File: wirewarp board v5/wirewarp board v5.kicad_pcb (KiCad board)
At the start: 2 copper layers, 99.1 x 99.1 mm, 1406 parts

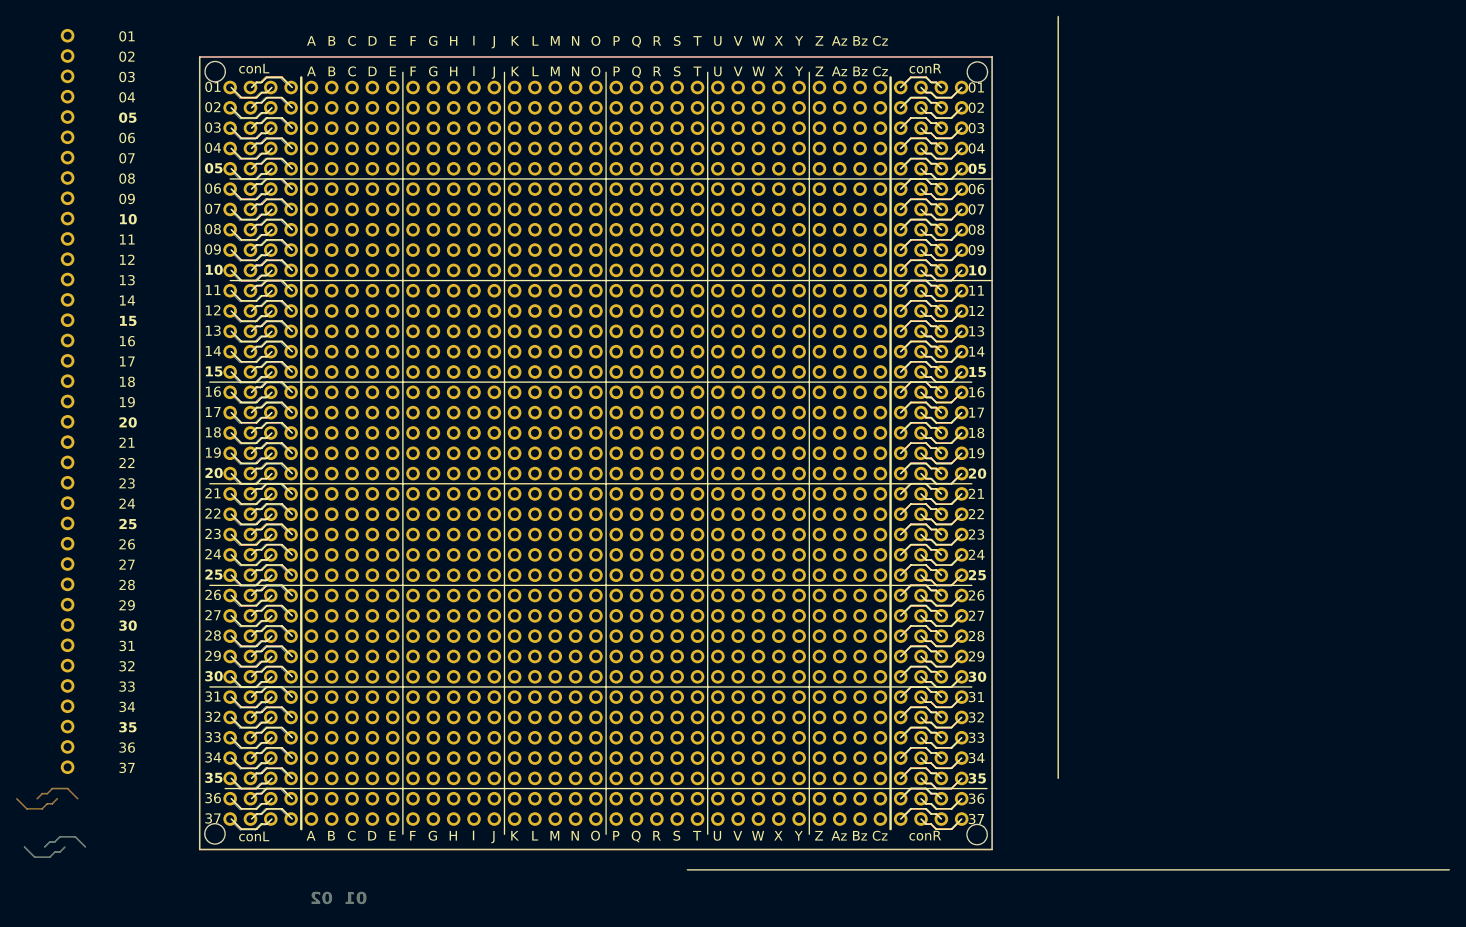
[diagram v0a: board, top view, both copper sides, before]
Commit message: update protoboard V, connectors at sides connected
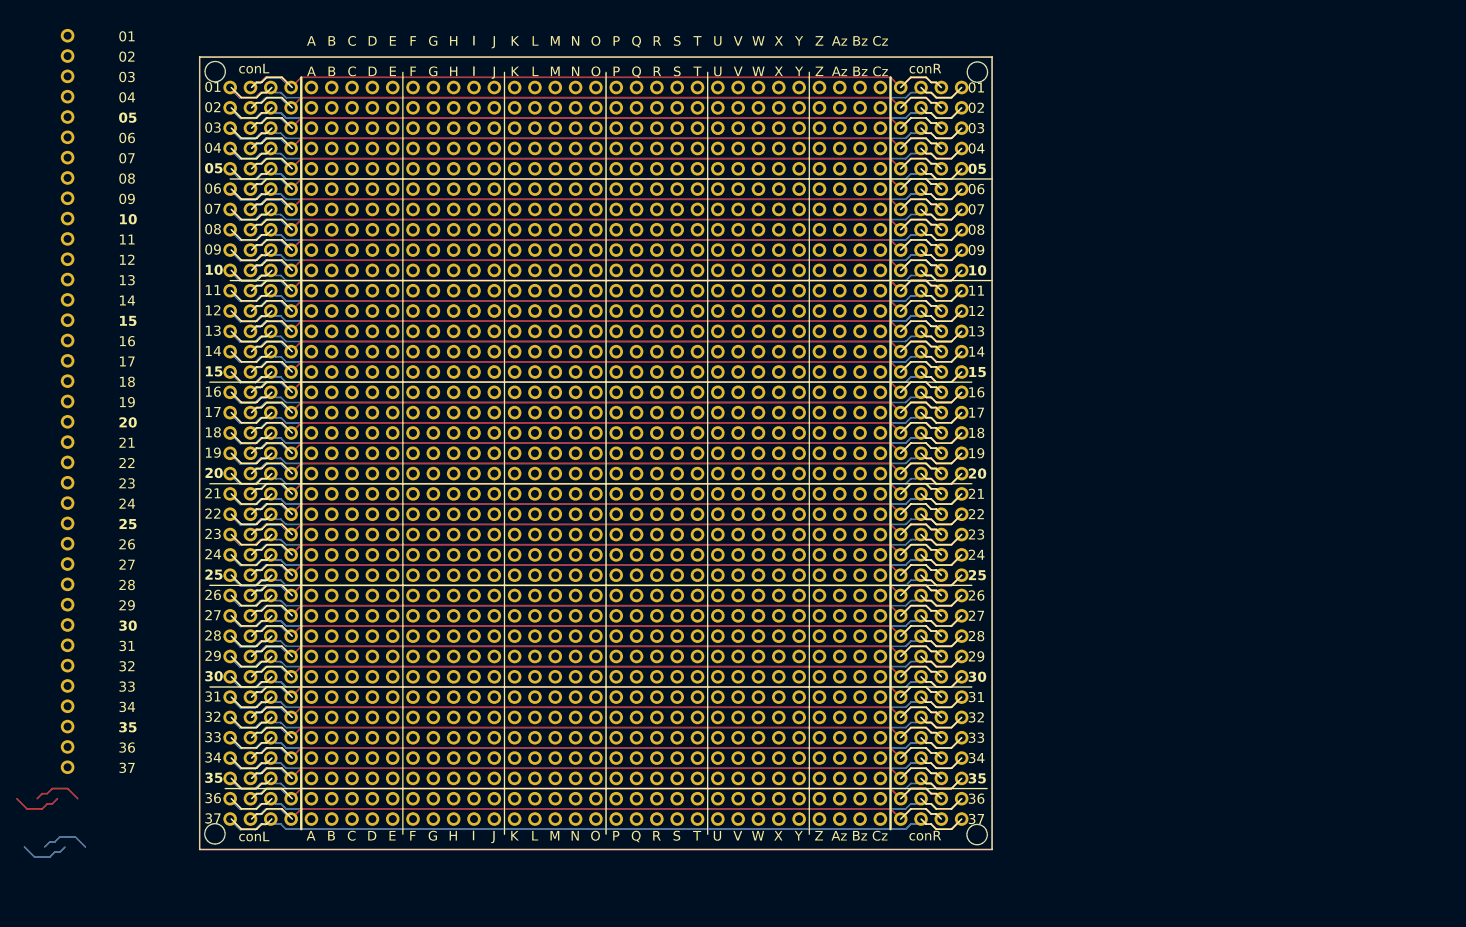
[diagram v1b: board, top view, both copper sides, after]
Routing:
- net (no net): track 3225.5 -> 9130.1 mm
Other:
- board text removed: "01 02"
